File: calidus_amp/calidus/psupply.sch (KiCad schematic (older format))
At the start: 49 parts, among them U1 LM317_3PinPackage, U2 LM337_TO220, U3 L7815, U4 L7805, U5 L7915

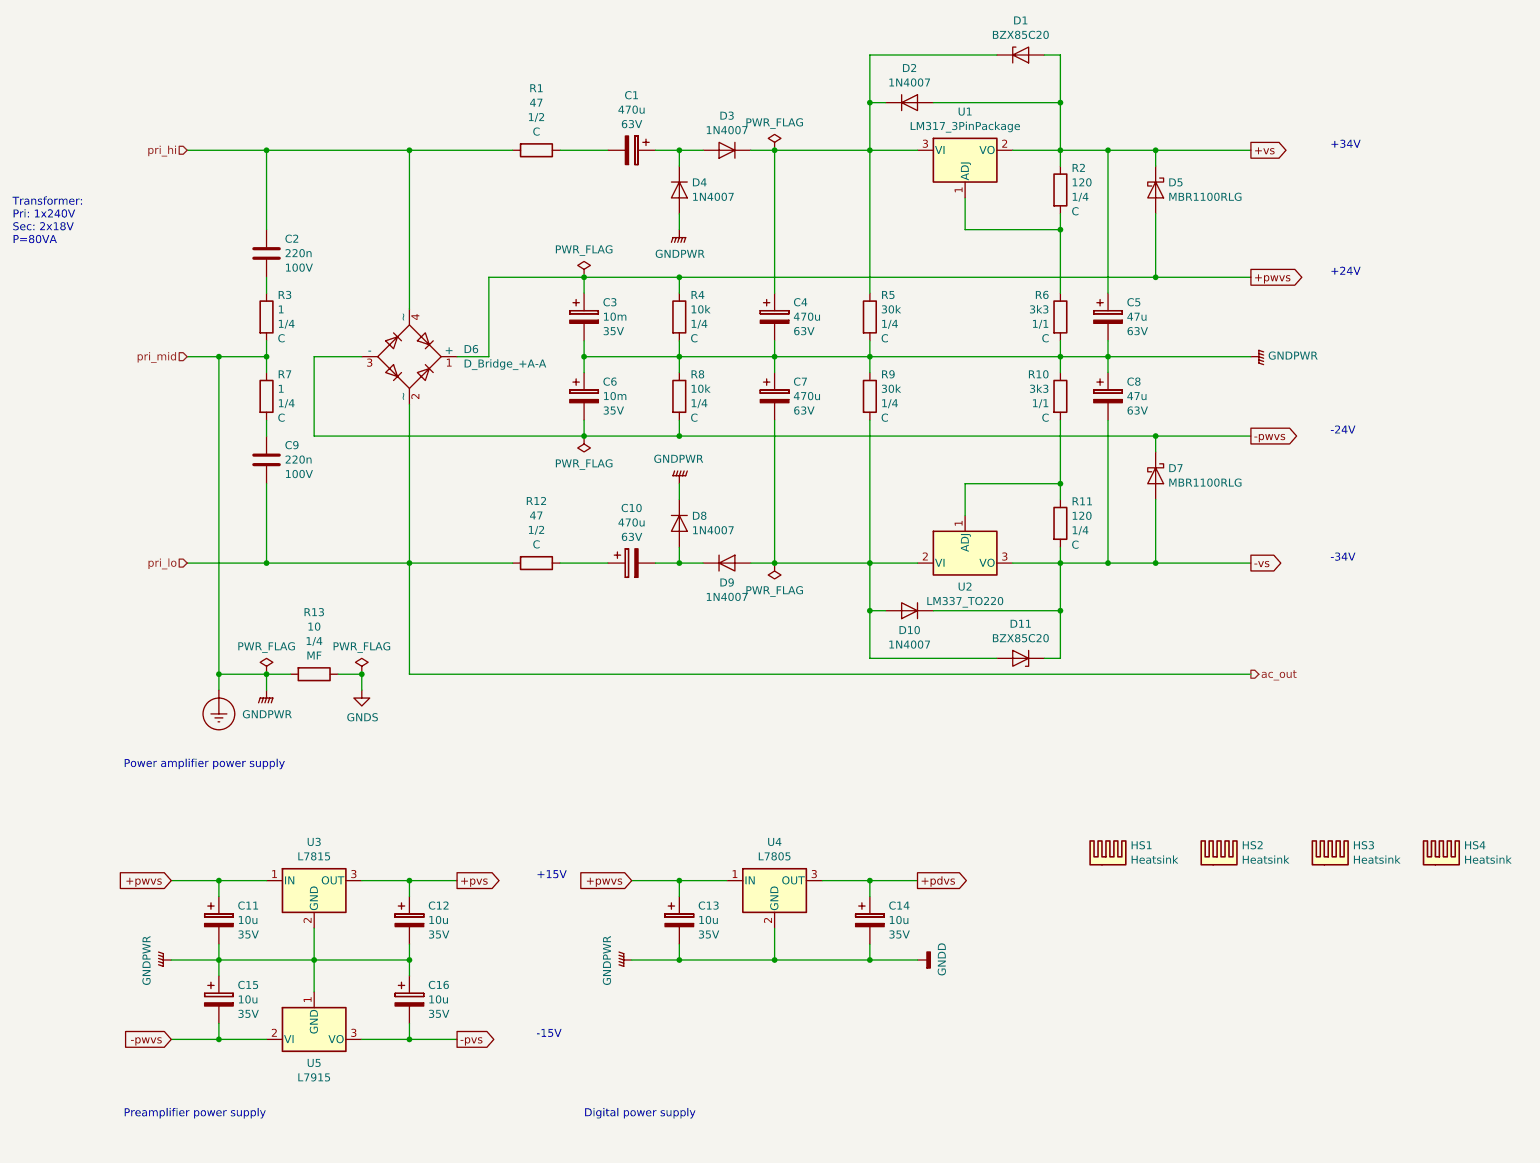
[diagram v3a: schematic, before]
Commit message: Updated schematic and footprinted Rybicon capacitors
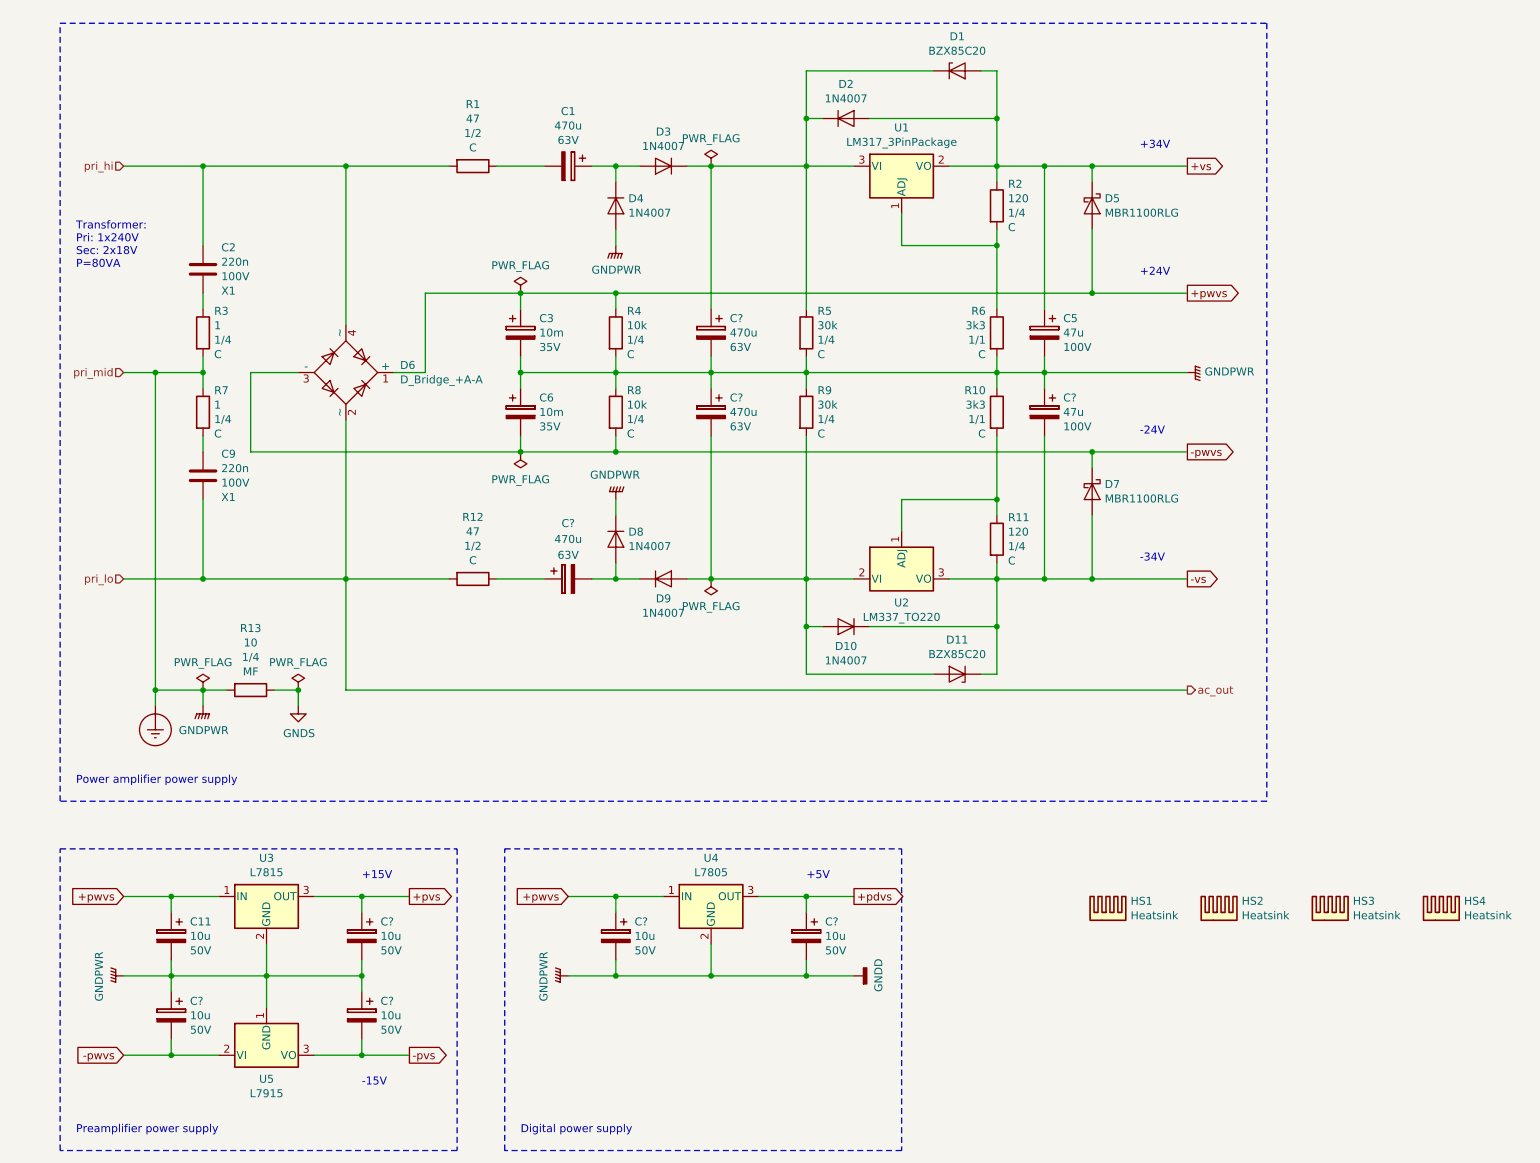
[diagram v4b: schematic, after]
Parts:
- removed C10, C4, C7: 470u, symbol Device:CP
- removed C12, C13, C14, C15, C16: 10u, symbol Device:CP
- removed C8: 47u, symbol Device:CP
- added C? (x5): 10u, Capacitor_THT:CP_Radial_D5.0mm_P2.00mm, symbol Device:CP
- added C?: 47u, Capacitor_THT:CP_Radial_D10.0mm_P5.00mm, symbol Device:CP
- added C? (x3): 470u, Capacitor_THT:CP_Radial_D12.5mm_P5.00mm, symbol Device:CP
- C1: footprint (none) -> Capacitor_THT:CP_Radial_D12.5mm_P5.00mm; Manufacturer (none) -> Rybicon:63YXF470MEFC12.5X25; Supplier (none) -> Farnell:1144639
- C11: footprint (none) -> Capacitor_THT:CP_Radial_D5.0mm_P2.00mm; Manufacturer (none) -> Rybicon:50YXF10MEFC5X11; Supplier1 (none) -> Farnell:1144632; Voltage 35V -> 50V
- C2, C9: Manufacturer (none) -> Kemet:PHE844RD6220MR06L2; Supplier (none) -> Farnell:2943922; Type (none) -> X1
- C5: footprint (none) -> Capacitor_THT:CP_Radial_D10.0mm_P5.00mm; Manufacturer (none) -> Rybicon:100YXF47MEFC10X16; Supplier1 (none) -> Farnell:1144641; Voltage 63V -> 100V
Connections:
- net +pdvs: now also C?.1
- net +pvs: now also C?.1
- net +pwvs: now also C?.1
- net -pvs: now also C?.2
- net -pwvs: now also C?.2
- net -vs: now also C?.2
- net Earth_Protective: now also C?.1, C?.1, C?.1, C?.1, C?.2, C?.2, C?.2, C?.2
- net at R12.1: now also C?.1
- net at D1.1 (K), D2.1 (K), D3.1 (K)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: now also C?.1
- net at D10.2 (A), D11.2 (A), D9.2 (A)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: now also C?.2
- net at D8.2 (A), D9.1 (K): now also C?.2
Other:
- note added: "+5V"
- moved on the sheet: C1, C11, C2, C3, C5, C6, D1, D10, D11, D2, D3, D4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

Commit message: Annotated the schematic
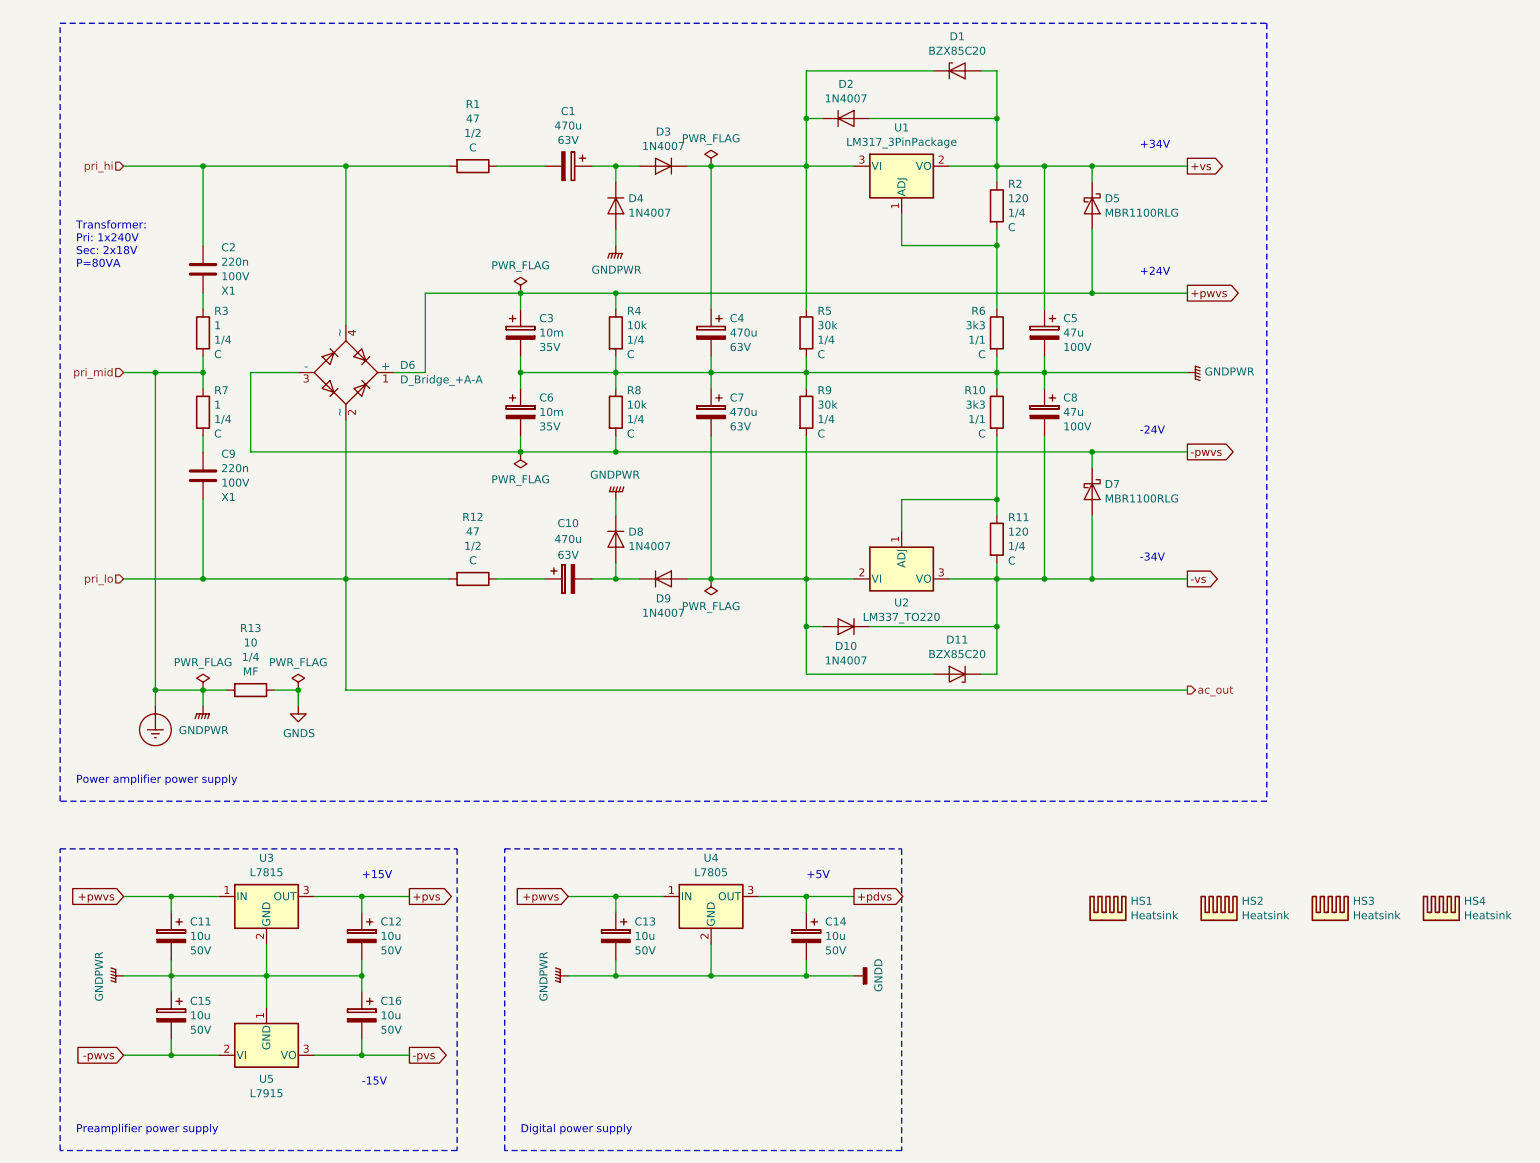
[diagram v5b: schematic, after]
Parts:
- gave numbers to parts that had none: 9
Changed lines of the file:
@@
 $EndComp
 $Comp
-L Device:CP C?
+L Device:CP C15
 U 1 1 5C5979FA
 P 2100 6850
-F 0 "C?" H 1982 6941 50  0000 R CNN
+F 0 "C15" H 1982 6941 50  0000 R CNN
 F 1 "10u" H 1982 6850 50  0000 R CNN
 F 2 "Capacitor_THT:CP_Radial_D5.0mm_P2.00mm" H 2138 6700 50  0001 C CNN
@@
 $EndComp
 $Comp
-L Device:CP C?
+L Device:CP C12
 U 1 1 5C5A56EF
 P 3300 6350
-F 0 "C?" H 3182 6441 50  0000 R CNN
+F 0 "C12" H 3182 6441 50  0000 R CNN
 F 1 "10u" H 3182 6350 50  0000 R CNN
 F 2 "Capacitor_THT:CP_Radial_D5.0mm_P2.00mm" H 3338 6200 50  0001 C CNN
@@
 $EndComp
 $Comp
-L Device:CP C?
+L Device:CP C16
 U 1 1 5C5A577F
 P 3300 6850
-F 0 "C?" H 3182 6941 50  0000 R CNN
+F 0 "C16" H 3182 6941 50  0000 R CNN
 F 1 "10u" H 3182 6850 50  0000 R CNN
 F 2 "Capacitor_THT:CP_Radial_D5.0mm_P2.00mm" H 3338 6700 50  0001 C CNN
@@
 $EndComp
 $Comp
-L Device:CP C?
+L Device:CP C13
 U 1 1 5C5A5803
 P 4900 6350
-F 0 "C?" H 4782 6441 50  0000 R CNN
+F 0 "C13" H 4782 6441 50  0000 R CNN
 F 1 "10u" H 4782 6350 50  0000 R CNN
 F 2 "Capacitor_THT:CP_Radial_D5.0mm_P2.00mm" H 4938 6200 50  0001 C CNN
@@
 $EndComp
 $Comp
-L Device:CP C?
+L Device:CP C14
 U 1 1 5C5A58A1
 P 6100 6350
-F 0 "C?" H 5982 6441 50  0000 R CNN
+F 0 "C14" H 5982 6441 50  0000 R CNN
 F 1 "10u" H 5982 6350 50  0000 R CNN
 F 2 "Capacitor_THT:CP_Radial_D5.0mm_P2.00mm" H 6138 6200 50  0001 C CNN
@@
 $EndComp
 $Comp
-L Device:CP C?
+L Device:CP C8
 U 1 1 5C5B32B4
 P 7600 3050
-F 0 "C?" H 7482 3141 50  0000 R CNN
+F 0 "C8" H 7482 3141 50  0000 R CNN
 F 1 "47u" H 7482 3050 50  0000 R CNN
 F 2 "Capacitor_THT:CP_Radial_D10.0mm_P5.00mm" H 7638 2900 50  0001 C CNN
@@
 $EndComp
 $Comp
-L Device:CP C?
+L Device:CP C4
 U 1 1 5C5DD036
 P 5500 2550
-F 0 "C?" H 5382 2641 50  0000 R CNN
+F 0 "C4" H 5382 2641 50  0000 R CNN
 F 1 "470u" H 5382 2550 50  0000 R CNN
 F 2 "Capacitor_THT:CP_Radial_D12.5mm_P5.00mm" H 5538 2400 50  0001 C CNN
@@
 $EndComp
 $Comp
-L Device:CP C?
+L Device:CP C7
 U 1 1 5C5E3E3F
 P 5500 3050
-F 0 "C?" H 5382 3141 50  0000 R CNN
+F 0 "C7" H 5382 3141 50  0000 R CNN
 F 1 "470u" H 5382 3050 50  0000 R CNN
 F 2 "Capacitor_THT:CP_Radial_D12.5mm_P5.00mm" H 5538 2900 50  0001 C CNN
@@
 $EndComp
 $Comp
-L Device:CP C?
+L Device:CP C10
 U 1 1 5C5E3ED1
 P 4600 4100
-F 0 "C?" V 4250 4100 50  0000 C CNN
+F 0 "C10" V 4250 4100 50  0000 C CNN
 F 1 "470u" V 4350 4100 50  0000 C CNN
 F 2 "Capacitor_THT:CP_Radial_D12.5mm_P5.00mm" H 4638 3950 50  0001 C CNN

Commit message: WIP: component footprint assignment.
Signed-off-by: Nenad Radulovic <nenad.b.radulovic@gmail.com>
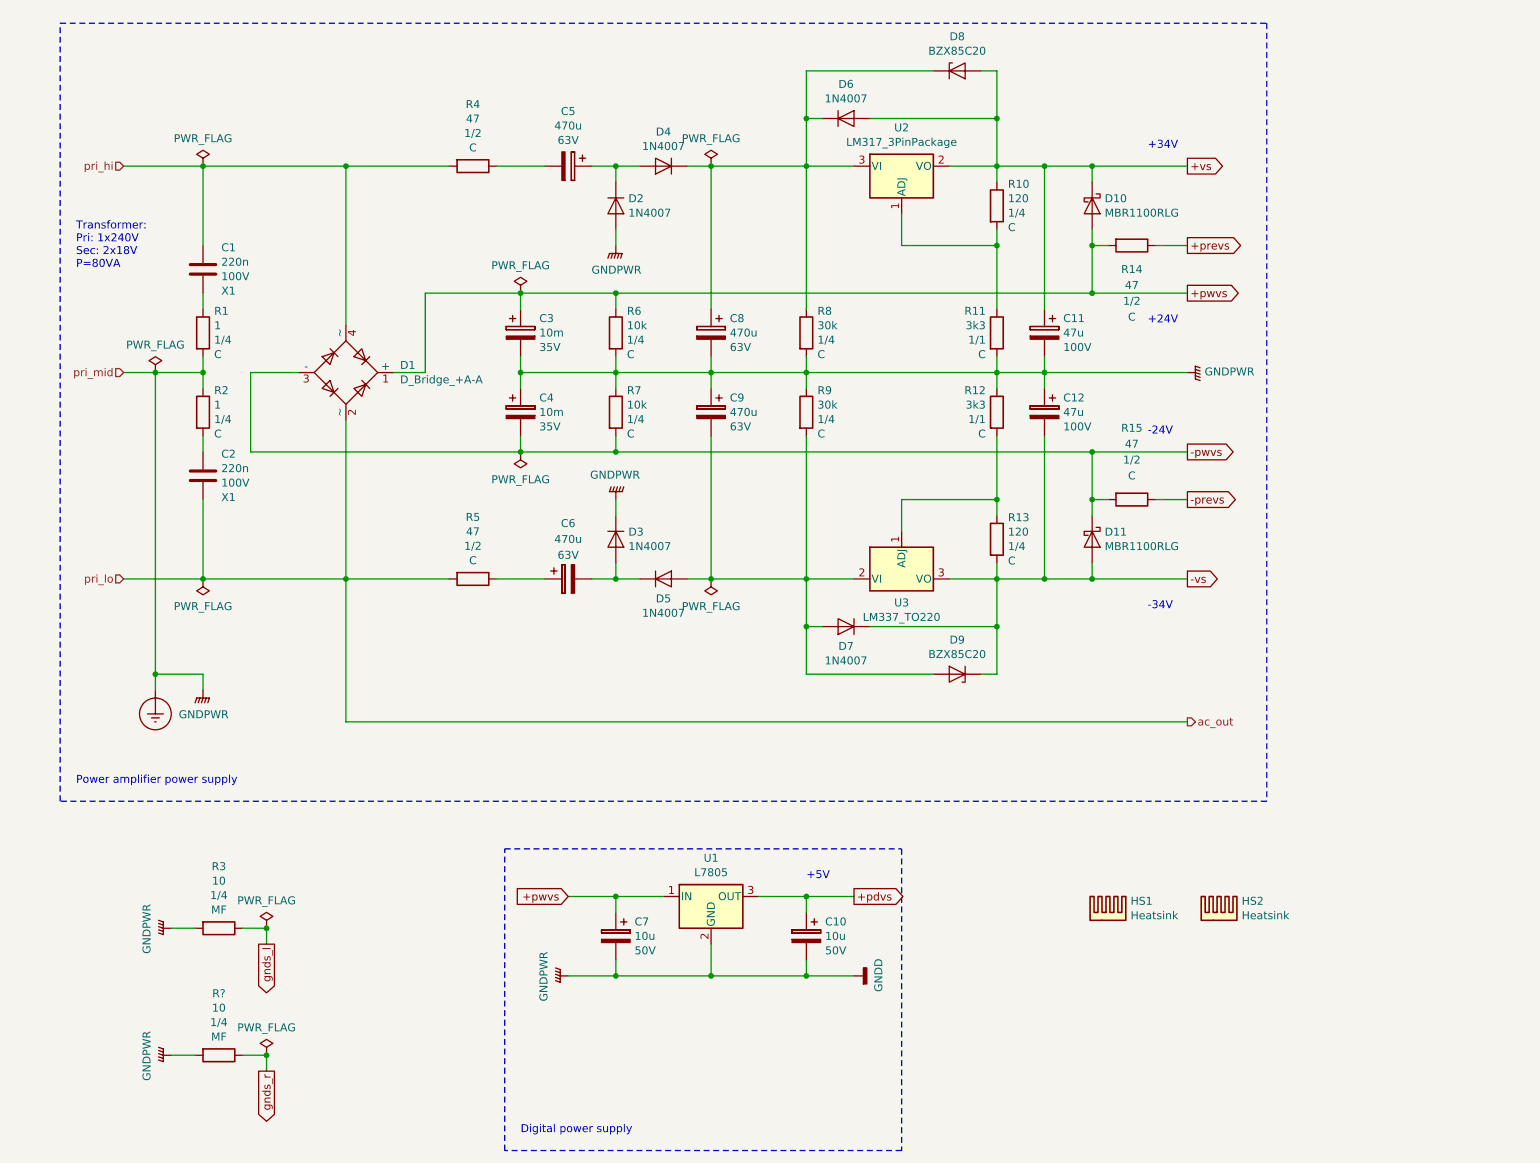
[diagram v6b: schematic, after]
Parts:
- removed C11, C12, C15, C16: 10u, Capacitor_THT:CP_Radial_D5.0mm_P2.00mm, symbol Device:CP
- removed HS3, HS4: Heatsink, Heatsink:Heatsink_Fischer_SK104-STCB_35x13mm__2xDrill3.5mm_ScrewM3, symbol Mechanical:Heatsink
- removed U3: L7815, Package_TO_SOT_THT:TO-220-3_Vertical, symbol Regulator_Linear:L7815
- removed U5: L7915, Package_TO_SOT_THT:TO-220-3_Vertical, symbol Regulator_Linear:L7915
- added R14, R15: 47, Resistor_THT:R_Axial_DIN0309_L9.0mm_D3.2mm_P12.70mm_Horizontal, symbol Device:R
- added R?: 10, Resistor_THT:R_Axial_DIN0207_L6.3mm_D2.5mm_P10.16mm_Horizontal, symbol Device:R
- C1: renamed from C2; footprint (none) -> Capacitor_THT:C_Rect_L19.0mm_W8.0mm_P15.00mm_MKS4
- C2: renamed from C9; footprint (none) -> Capacitor_THT:C_Rect_L19.0mm_W8.0mm_P15.00mm_MKS4
- C3: footprint (none) -> Capacitor_THT:CP_Radial_D30.0mm_P10.00mm_SnapIn
- C4: renamed from C6; footprint (none) -> Capacitor_THT:CP_Radial_D30.0mm_P10.00mm_SnapIn
- D1: renamed from D6; footprint (none) -> Diode_THT:Diode_Bridge_32.0x5.6x17.0mm_P10.0mm_P7.5mm
- D10: renamed from D5; footprint (none) -> Diode_THT:D_DO-41_SOD81_P7.62mm_Horizontal
- D11: renamed from D7; footprint (none) -> Diode_THT:D_DO-41_SOD81_P7.62mm_Horizontal
- D2: renamed from D4; footprint (none) -> Diode_THT:D_DO-41_SOD81_P7.62mm_Horizontal
- D3: renamed from D8; footprint (none) -> Diode_THT:D_DO-41_SOD81_P7.62mm_Horizontal
- D4: renamed from D3; footprint (none) -> Diode_THT:D_DO-41_SOD81_P7.62mm_Horizontal
- D5: renamed from D9; footprint (none) -> Diode_THT:D_DO-41_SOD81_P7.62mm_Horizontal
- D6: renamed from D2; footprint (none) -> Diode_THT:D_DO-41_SOD81_P7.62mm_Horizontal
- D7: renamed from D10; footprint (none) -> Diode_THT:D_DO-41_SOD81_P7.62mm_Horizontal
- D8: renamed from D1; footprint (none) -> Diode_THT:D_DO-41_SOD81_P7.62mm_Horizontal
- D9: renamed from D11; footprint (none) -> Diode_THT:D_DO-41_SOD81_P7.62mm_Horizontal
- R1: renamed from R3; footprint (none) -> Resistor_THT:R_Axial_DIN0207_L6.3mm_D2.5mm_P7.62mm_Horizontal
- R10: renamed from R2; footprint (none) -> Resistor_THT:R_Axial_DIN0207_L6.3mm_D2.5mm_P10.16mm_Horizontal
- R11: renamed from R6; footprint (none) -> Resistor_THT:R_Axial_DIN0309_L9.0mm_D3.2mm_P12.70mm_Horizontal
- R12: renamed from R10; footprint (none) -> Resistor_THT:R_Axial_DIN0309_L9.0mm_D3.2mm_P12.70mm_Horizontal
- R13: renamed from R11; footprint (none) -> Resistor_THT:R_Axial_DIN0207_L6.3mm_D2.5mm_P10.16mm_Horizontal
- R2: renamed from R7; footprint (none) -> Resistor_THT:R_Axial_DIN0207_L6.3mm_D2.5mm_P7.62mm_Horizontal
- R3: renamed from R13; footprint (none) -> Resistor_THT:R_Axial_DIN0207_L6.3mm_D2.5mm_P10.16mm_Horizontal
- R4: renamed from R1; footprint (none) -> Resistor_THT:R_Axial_DIN0309_L9.0mm_D3.2mm_P12.70mm_Horizontal
- R5: renamed from R12; footprint (none) -> Resistor_THT:R_Axial_DIN0309_L9.0mm_D3.2mm_P12.70mm_Horizontal
- R6: renamed from R4; footprint (none) -> Resistor_THT:R_Axial_DIN0207_L6.3mm_D2.5mm_P10.16mm_Horizontal
- R7: renamed from R8; footprint (none) -> Resistor_THT:R_Axial_DIN0207_L6.3mm_D2.5mm_P10.16mm_Horizontal
- R8: renamed from R5; footprint (none) -> Resistor_THT:R_Axial_DIN0207_L6.3mm_D2.5mm_P10.16mm_Horizontal
- R9: footprint (none) -> Resistor_THT:R_Axial_DIN0207_L6.3mm_D2.5mm_P10.16mm_Horizontal
- renumbered C14 to C10, C5 to C11, C8 to C12, C1 to C5, C10 to C6, C13 to C7, C4 to C8, C7 to C9, U4 to U1, U1 to U2, U2 to U3
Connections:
- net +pwvs: now also R14.2
- net -pwvs: now also R15.2
- net Earth_Protective: now also R?.2
- net GNDS renamed gnds_l
- new net +prevs: R14.1
- new net -prevs: R15.1
- new net gnds_r: R?.1
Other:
- note removed: "+15V"
- note removed: "-15V"
- note removed: "Preamplifier power supply"
- moved on the sheet: D11, R3
